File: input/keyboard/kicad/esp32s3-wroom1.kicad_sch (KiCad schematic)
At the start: 22 parts, among them J1 Conn_01x01_Pin, J10 Conn_01x01_Pin, J11 USB_C_Receptacle_USB2.0_16P, J12 Conn_01x02_Pin, J13 Conn_01x16_Pin, J14 Conn_01x04_Pin, J2 Conn_01x01_Pin, J3 Conn_01x01_Pin, J4 Conn_01x01_Pin, J5 Conn_01x01_Pin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

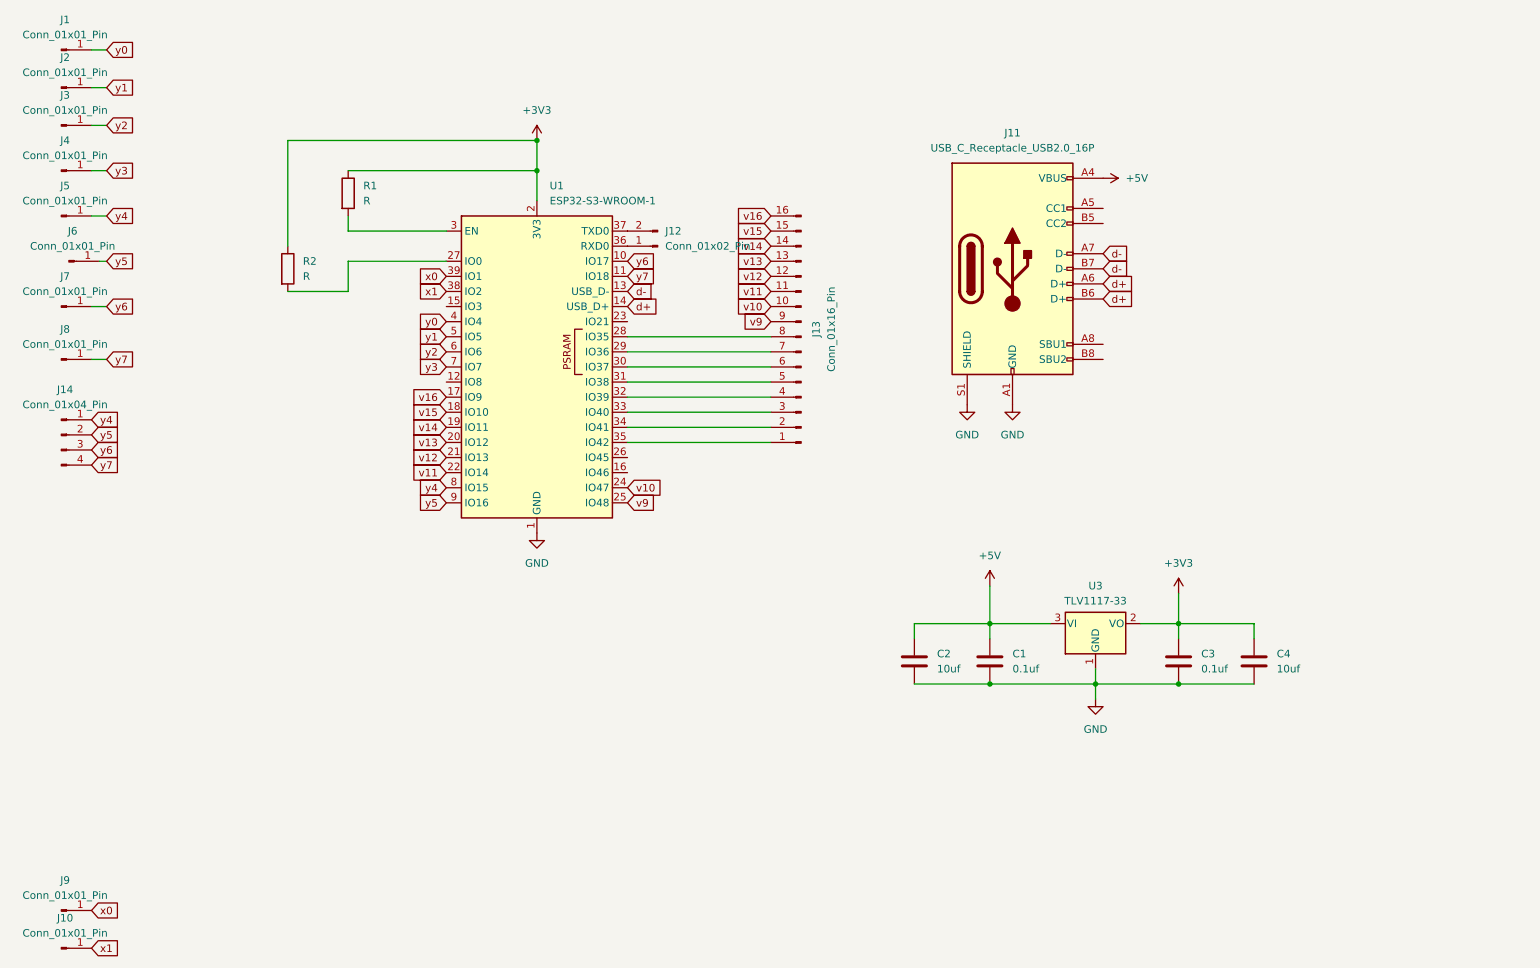
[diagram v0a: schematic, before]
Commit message: reorganize dir, keyboard pcb update
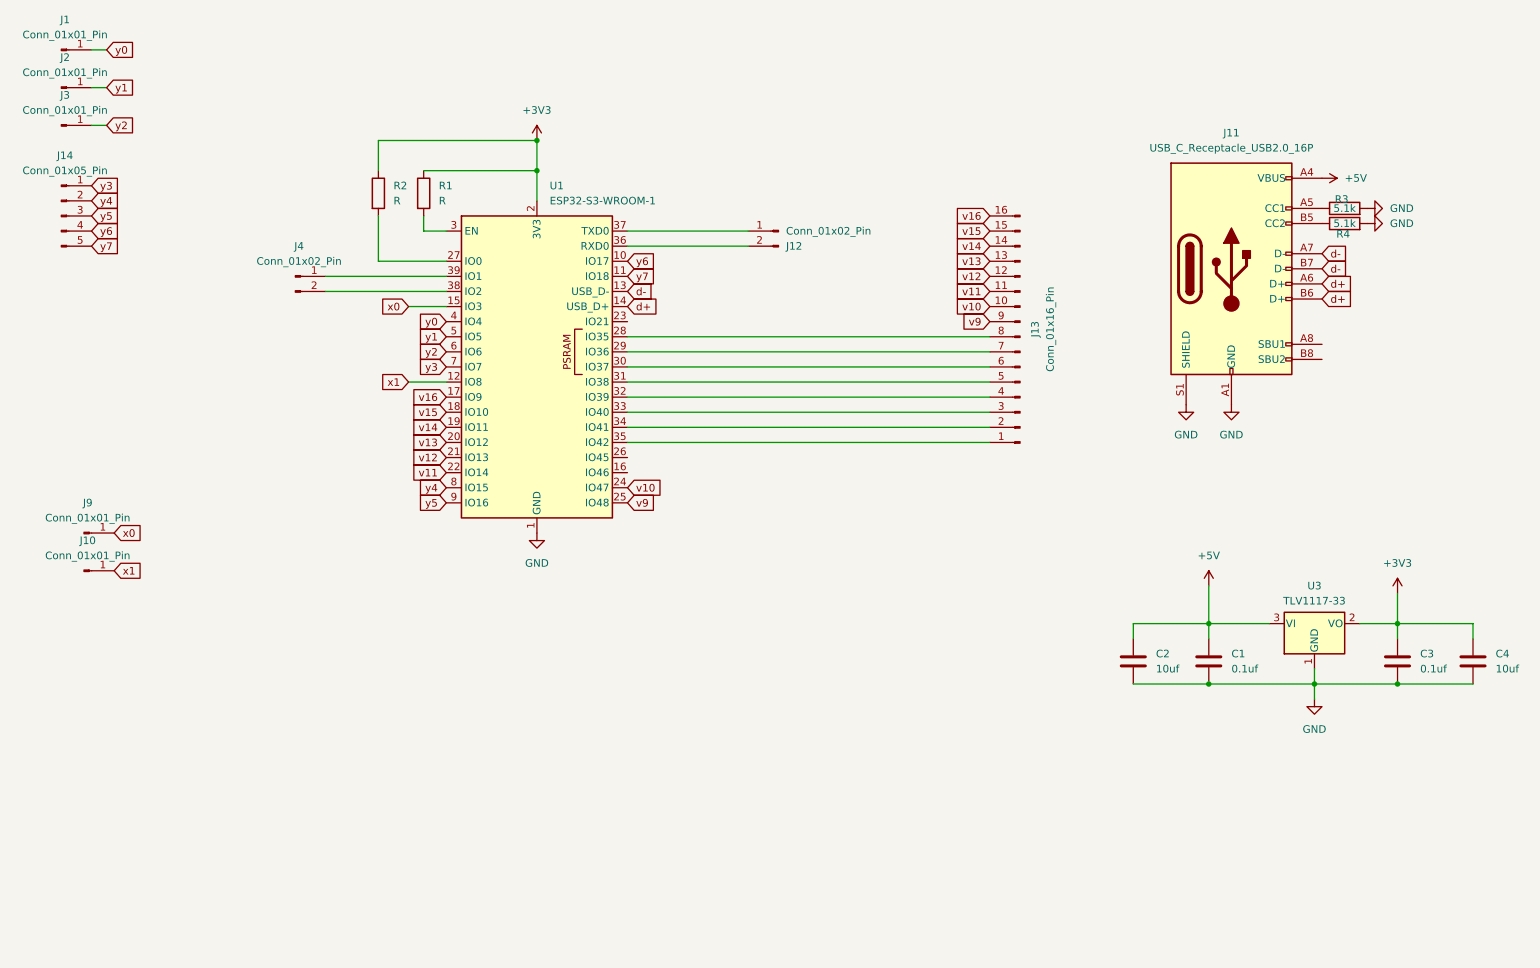
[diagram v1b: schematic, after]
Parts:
- removed J14: Conn_01x04_Pin, Connector_PinHeader_2.54mm:PinHeader_1x04_P2.54mm_Vertical, symbol Connector:Conn_01x04_Pin
- removed J4, J5, J6, J7, J8: Conn_01x01_Pin, Connector_PinHeader_2.54mm:PinHeader_1x01_P2.54mm_Vertical, symbol Connector:Conn_01x01_Pin
- added J14: Conn_01x05_Pin, Connector_PinHeader_2.54mm:PinHeader_1x05_P2.54mm_Vertical, symbol Connector:Conn_01x05_Pin
- added J4: Conn_01x02_Pin, Connector_PinHeader_2.54mm:PinHeader_1x02_P2.54mm_Vertical, symbol Connector:Conn_01x02_Pin
- added R3, R4: 5.1k, Resistor_SMD:R_0805_2012Metric, symbol Device:R
- J13: footprint Connector_PinSocket_1.27mm:PinSocket_1x16_P1.27mm_Vertical -> Connector_PinHeader_2.54mm:PinHeader_1x16_P2.54mm_Vertical
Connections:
- net GND: now also R3.2, R4.2
- net x0: now also U1.15 (IO3); no longer U1.39 (IO1)
- net x1: now also U1.12 (IO8); no longer U1.38 (IO2)
- net y3: now also J14.1 (Pin_1)
- net y4: now also J14.2 (Pin_2)
- net y5: now also J14.3 (Pin_3)
- net y6: now also J14.4 (Pin_4)
- net y7: now also J14.5 (Pin_5)
- net at U1.36 (RXD0): now also J12.2 (Pin_2); no longer J12.1 (Pin_1)
- net at U1.37 (TXD0): now also J12.1 (Pin_1); no longer J12.2 (Pin_2)
- net at J11.A5 (CC1): now also R3.1
- net at J11.B5 (CC2): now also R4.1
- new net: J4.2 (Pin_2), U1.38 (IO2)
- new net: J4.1 (Pin_1), U1.39 (IO1)
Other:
- moved on the sheet: C1, C2, C3, C4, J10, J11, J12, J13, J9, R1, R2, U3
